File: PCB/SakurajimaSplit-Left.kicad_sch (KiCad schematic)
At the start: 53 parts, among them J1 SWD, J10 Conn_01x01_Pin, J11 Conn_01x01_Pin, J12 Conn_01x01_Pin, J13 Conn_01x01_Pin, J14 Conn_01x01_Pin, J15 Conn_01x01_Pin, J16 Conn_01x01_Pin, J17 Conn_01x01_Pin, J18 Conn_01x01_Pin, J2 USB-C to Right-Half, J3 Conn_01x01_Pin, J4 Conn_01x01_Pin, J5 Conn_01x01_Pin, J6 Conn_01x01_Pin, J7 Conn_01x01_Pin, J8 Conn_01x01_Pin, J9 Conn_01x01_Pin, SW1 SWCLK/BOOT0, SW2 Knob, U1 USBLC6-2SC6, U2 STM32G0B1CBT6, U3 ZJY_M233, Y1 8MHz

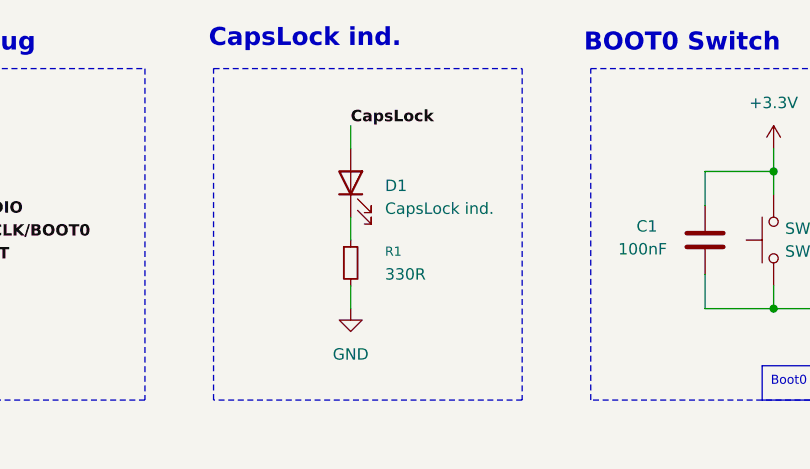
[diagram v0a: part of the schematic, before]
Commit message: fix(sch): fix matrix diode designators not starting from 1
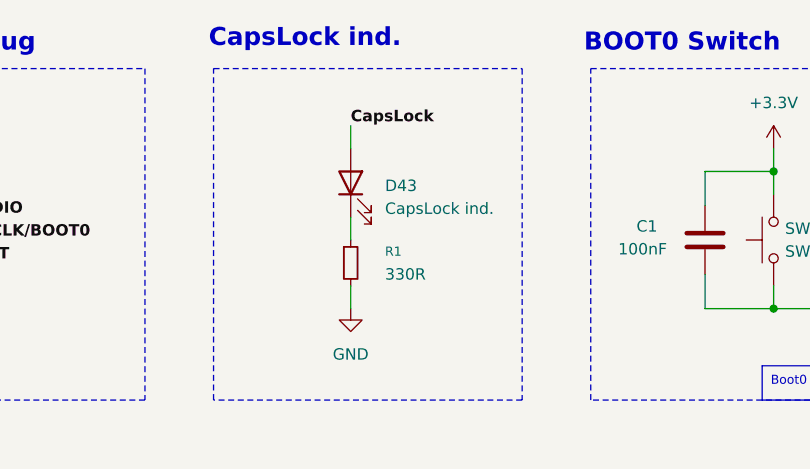
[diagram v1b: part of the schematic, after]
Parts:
- renumbered D1 to D43
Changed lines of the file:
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@@
 		(dnp no)
 		(fields_autoplaced yes)
-		(property "Reference" "D1"
+		(property "Reference" "D43"
 			(at 91.44 40.9574 90)
 			(effects
@@
 			(project ""
 				(path "/2049b6de-7453-46e1-ab60-70116abff9d6/d08add9a-e5d5-49be-809e-a90adb11436d"
-					(reference "D1")
+					(reference "D43")
 					(unit 1)
 				)

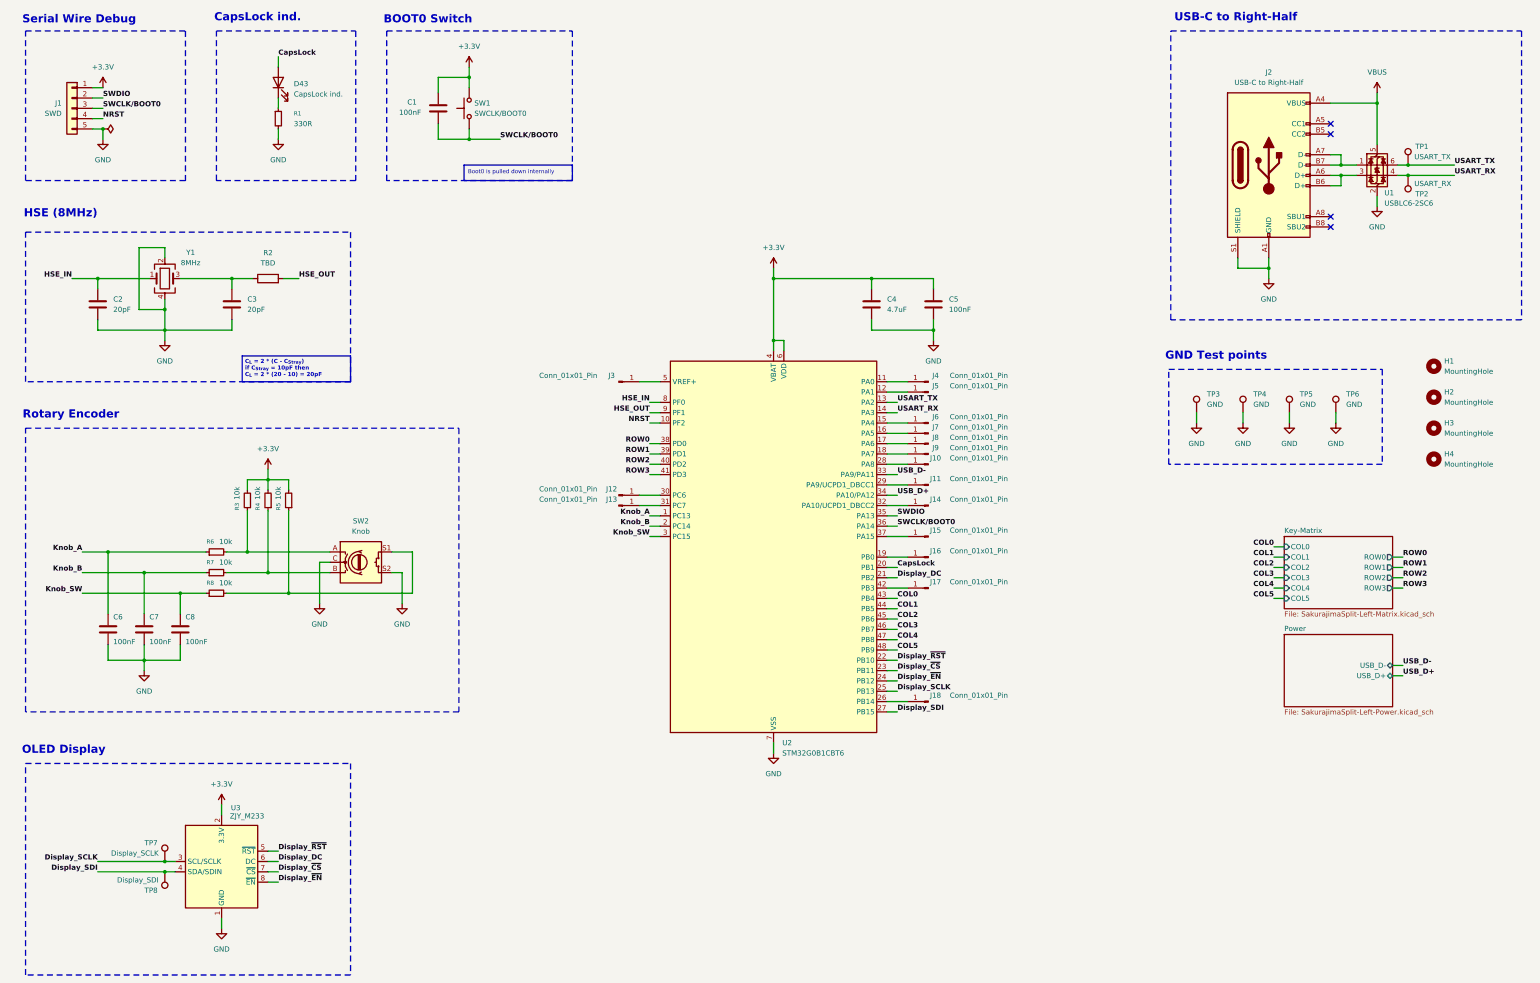
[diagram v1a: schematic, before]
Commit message: feat(sch): add spi flash, remove rotary encoder, fix footprints
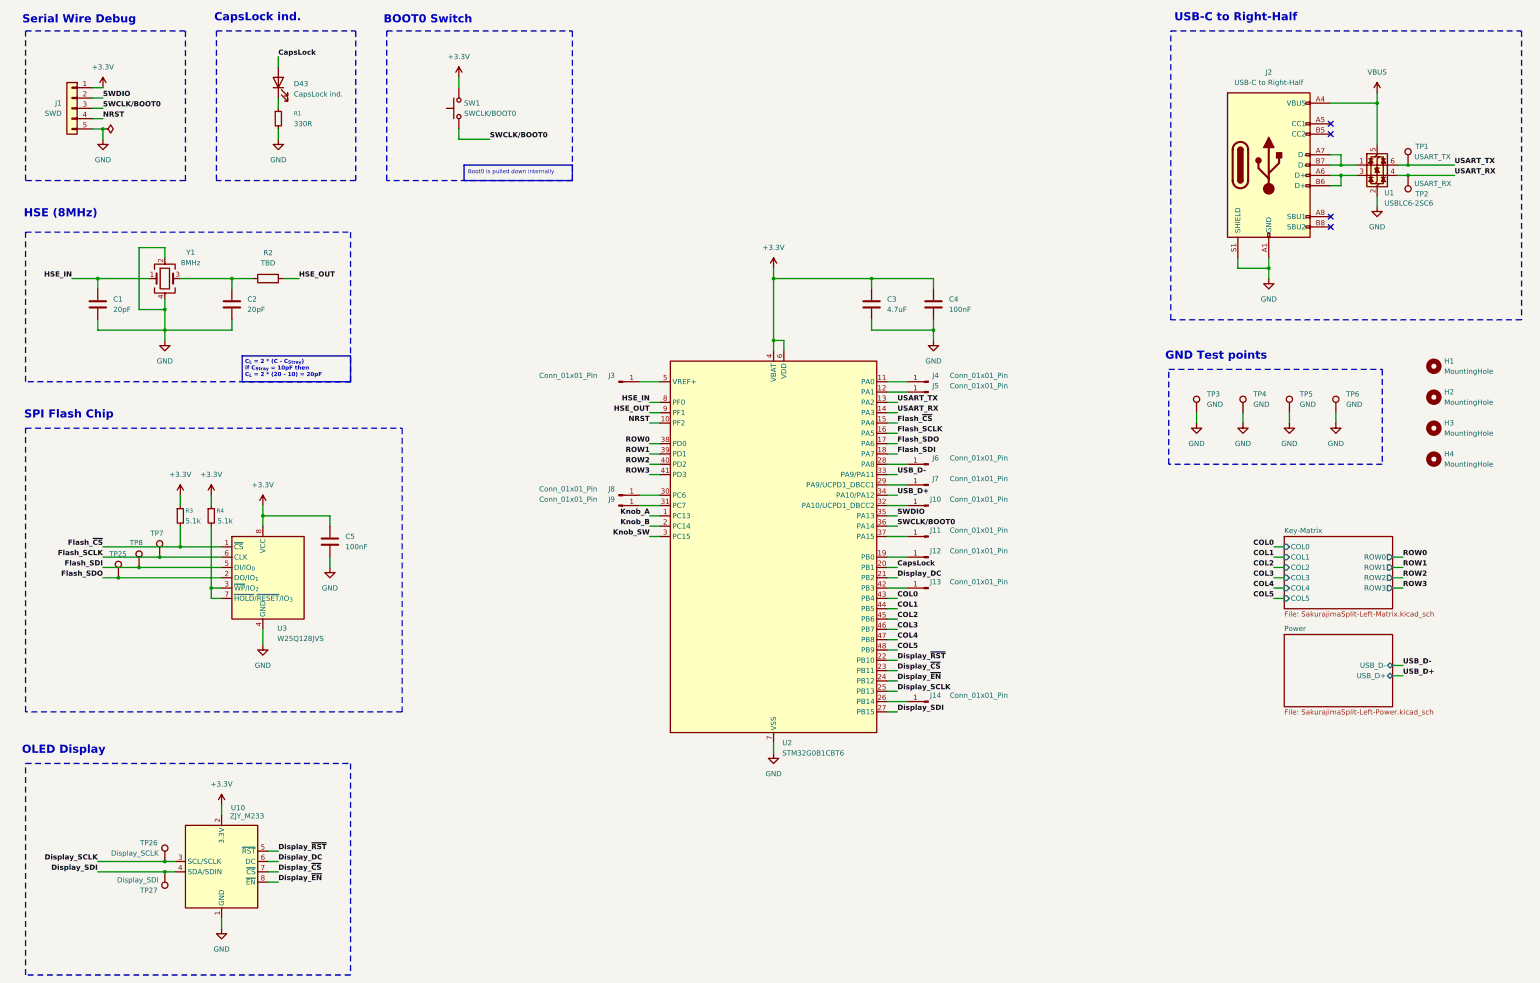
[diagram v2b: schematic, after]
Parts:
- removed C1, C6, C7, C8: 100nF, Capacitor_SMD:C_0603_1608Metric, symbol Device:C
- removed J6, J7, J8, J9: Conn_01x01_Pin, Connector_Wire:SolderWirePad_1x01_SMD_1x2mm, symbol Connector:Conn_01x01_Pin
- removed R5, R6, R7, R8: 10k, Resistor_SMD:R_0603_1608Metric, symbol Device:R_Small
- removed SW2: Knob, Rotary_Encoder:RotaryEncoder_Alps_EC11E-Switch_Vertical_H20mm, symbol Device:RotaryEncoder_Switch
- added C5: 100nF, Capacitor_SMD:C_0603_1608Metric, symbol Device:C
- added TP25: Flash_SDO, Hayata_Lib:TestPoint_Pad_Circular_1.3mm, symbol Connector:TestPoint
- added TP7: Flash_SCLK, Hayata_Lib:TestPoint_Pad_Circular_1.3mm, symbol Connector:TestPoint
- added TP8: Flash_SDI, Hayata_Lib:TestPoint_Pad_Circular_1.3mm, symbol Connector:TestPoint
- added U3: W25Q128JVS, Package_SO:SOIC-8_5.3x5.3mm_P1.27mm, symbol Memory_Flash:W25Q128JVS
- R3, R4: value 10k -> 5.1k; Distributor Link https://lionelectronic.ir/products/1219-CR0603FA1002G -> https://lionelectronic.ir/products/1212-0603WAF5101T5E; Manufacturer LIZ Electronics -> UniOhm; Manufacturer Part No. CR0603FA1002G -> 0603WAF5101T5E
- SW1: footprint Button_Switch_SMD:SW_Push_1P1T_XKB_TS-1187A -> Hayata_Lib:SW_Push_TS-1010B
- TP1, TP2, TP3, TP4, TP5, TP6: footprint TestPoint:TestPoint_Pad_2.0x2.0mm -> Hayata_Lib:TestPoint_Pad_Circular_1.3mm
- TP26: renamed from TP7; footprint TestPoint:TestPoint_Pad_2.0x2.0mm -> Hayata_Lib:TestPoint_Pad_Circular_1.3mm
- TP27: renamed from TP8; footprint TestPoint:TestPoint_Pad_2.0x2.0mm -> Hayata_Lib:TestPoint_Pad_Circular_1.3mm
- Y1: footprint Crystal:Crystal_SMD_3225-4Pin_3.2x2.5mm_HandSoldering -> Crystal:Crystal_SMD_3225-4Pin_3.2x2.5mm
- renumbered C2 to C1, C3 to C2, C4 to C3, C5 to C4, J14 to J10, J15 to J11, J16 to J12, J17 to J13, J18 to J14, J10 to J6, J11 to J7, J12 to J8, J13 to J9, U3 to U10
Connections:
- net +3.3V: now also R3.1, R4.1, C5.1, U3.8 (VCC); no longer R3.2, R4.2
- net GND: now also C5.2, U3.4 (GND)
- net Flash_~{CS}: now reaches U2.15 (PA4)
- net Flash_~{CS}: now also R3.2, U3.1 (~{CS})
- net Flash_SCLK: now reaches U2.16 (PA5)
- net Flash_SCLK: now also TP7.1, U3.6 (CLK)
- net Flash_SDO: now reaches U2.17 (PA6)
- net Flash_SDO: now also TP25.1, U3.2 (DO/IO_{1})
- net Flash_SDI: now reaches U2.18 (PA7)
- net Flash_SDI: now also TP8.1, U3.5 (DI/IO_{0})
- new net: R4.2, U3.3 (~{WP}/IO_{2}), U3.7 (~{HOLD}/~{RESET}/IO_{3})
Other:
- note added: "SPI Flash Chip"
- note removed: "Rotary Encoder"
- moved on the sheet: SW1

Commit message: fix(sch): remove encoder net labels, update mountinghole footprints
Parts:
- added J11, J12, J13: Conn_01x01_Pin, Connector_Wire:SolderWirePad_1x01_SMD_1x2mm, symbol Connector:Conn_01x01_Pin
- H1, H2, H3, H4: footprint MountingHole:MountingHole_3.2mm_M3_Pad -> MountingHole:MountingHole_3.2mm_M3_Pad_Via
- renumbered J11 to J14, J12 to J32, J13 to J33, J14 to J34
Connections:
- net Knob_A: no longer names the net of U2.1 (PC13)
- net Knob_A: now also J11.1 (Pin_1)
- net Knob_B: no longer names the net of U2.2 (PC14)
- net Knob_B: now also J12.1 (Pin_1)
- net Knob_SW: no longer names the net of U2.3 (PC15)
- net Knob_SW: now also J13.1 (Pin_1)
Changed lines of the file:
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@@
 	(wire
 		(pts
+			(xy 176.53 152.4) (xy 181.61 152.4)
+		)
+		(stroke
+			(width 0)
+			(type default)
+		)
+	)
+	(wire
+		(pts
 			(xy 71.12 165.1) (xy 71.12 167.64)
 		)
@@
 	(wire
 		(pts
-			(xy 179.07 149.86) (xy 181.61 149.86)
-		)
-		(stroke
-			(width 0)
-			(type default)
-		)
-	)
-	(wire
-		(pts
 			(xy 132.08 54.61) (xy 139.7 54.61)
 		)
@@
 	(wire
 		(pts
+			(xy 176.53 149.86) (xy 181.61 149.86)
+		)
+		(stroke
+			(width 0)
+			(type default)
+		)
+	)
+	(wire
+		(pts
 			(xy 87.63 44.45) (xy 87.63 46.99)
 		)
@@
 	(wire
 		(pts
+			(xy 176.53 147.32) (xy 181.61 147.32)
+		)
+		(stroke
+			(width 0)
+			(type default)
+		)
+	)
+	(wire
+		(pts
 			(xy 179.07 129.54) (xy 181.61 129.54)
 		)
@@
 	(wire
 		(pts
-			(xy 179.07 152.4) (xy 181.61 152.4)
-		)
-		(stroke
-			(width 0)
-			(type default)
-		)
-	)
-	(wire
-		(pts
 			(xy 358.14 45.72) (xy 358.14 55.88)
 		)
@@
 	(wire
 		(pts
-			(xy 179.07 147.32) (xy 181.61 147.32)
-		)
-		(stroke
-			(width 0)
-			(type default)
-		)
-	)
-	(wire
-		(pts
 			(xy 364.49 162.56) (xy 361.95 162.56)
 		)
@@
 		)
 	)
-	(label "Knob_SW"
-		(at 179.07 152.4 180)
-		(effects
-			(font
-				(size 1.27 1.27)
-				(thickness 0.254)
-				(bold yes)
-			)
-			(justify right bottom)
-		)
-	)
 	(label "COL0"
 		(at 332.74 154.94 180)
@@
 		)
 	)
-	(label "Knob_B"
-		(at 179.07 149.86 180)
-		(effects
-			(font
-				(size 1.27 1.27)
-				(thickness 0.254)
-				(bold yes)
-			)
-			(justify right bottom)
-		)
-	)
 	(label "ROW1"
 		(at 179.07 132.08 180)
@@
 		)
 	)
-	(label "Knob_A"
-		(at 179.07 147.32 180)
-		(effects
-			(font
-				(size 1.27 1.27)
-				(thickness 0.254)
-				(bold yes)
-			)
-			(justify right bottom)
-		)
-	)
 	(label "COL5"
 		(at 332.74 167.64 180)
@@
 			)
 		)
-		(property "Footprint" "MountingHole:MountingHole_3.2mm_M3_Pad"
+		(property "Footprint" "MountingHole:MountingHole_3.2mm_M3_Pad_Via"
 			(at 372.11 118.11 0)
 			(effects
@@
 		(on_board yes)
 		(dnp no)
-		(property "Reference" "J13"
+		(property "Reference" "J33"
 			(at 249.428 163.576 0)
 			(effects
@@
 			(project "SakurajimaSplit"
 				(path "/2049b6de-7453-46e1-ab60-70116abff9d6/d08add9a-e5d5-49be-809e-a90adb11436d"
-					(reference "J13")
+					(reference "J33")
 					(unit 1)
 				)
@@
 		(on_board yes)
 		(dnp no)
-		(property "Reference" "J12"
+		(property "Reference" "J32"
 			(at 249.428 155.956 0)
 			(effects
@@
 			(project "SakurajimaSplit"
 				(path "/2049b6de-7453-46e1-ab60-70116abff9d6/d08add9a-e5d5-49be-809e-a90adb11436d"
-					(reference "J12")
+					(reference "J32")
 					(unit 1)
 				)
@@
 		(on_board yes)
 		(dnp no)
-		(property "Reference" "J14"
+		(property "Reference" "J34"
 			(at 249.428 191.516 0)
 			(effects
@@
 			(project "SakurajimaSplit"
 				(path "/2049b6de-7453-46e1-ab60-70116abff9d6/d08add9a-e5d5-49be-809e-a90adb11436d"
-					(reference "J14")
+					(reference "J34")
 					(unit 1)
 				)
@@
 			)
 		)
-		(property "Footprint" "MountingHole:MountingHole_3.2mm_M3_Pad"
+		(property "Footprint" "MountingHole:MountingHole_3.2mm_M3_Pad_Via"
 			(at 372.11 110.49 0)
 			(effects
@@
 	)
 	(symbol
+		(lib_id "Connector:Conn_01x01_Pin")
+		(at 171.45 149.86 0)
+		(mirror x)
+		(unit 1)
+		(exclude_from_sim no)
+		(in_bom no)
+		(on_board yes)
+		(dnp no)
+		(property "Reference" "J12"
+			(at 169.672 148.336 0)
+			(effects
+				(font
+					(size 1.27 1.27)
+				)
+			)
+		)
+		(property "Value" "Conn_01x01_Pin"
+			(at 159.004 148.336 0)
+			(effects
+				(font
+					(size 1.27 1.27)
+				)
+			)
+		)
+		(property "Footprint" "Connector_Wire:SolderWirePad_1x01_SMD_1x2mm"
+			(at 171.45 149.86 0)
+			(effects
+				(font
+					(size 1.27 1.27)
+					(thickness 0.254)
+					(bold yes)
+				)
+				(hide yes)
+			)
+		)
+		(property "Datasheet" "~"
+			(at 171.45 149.86 0)
+			(effects
+				(font
+					(size 1.27 1.27)
+					(thickness 0.254)
+					(bold yes)
+				)
+				(hide yes)
+			)
+		)
+		(property "Description" "Generic connector, single row, 01x01, script generated"
+			(at 171.45 149.86 0)
+			(effects
+				(font
+					(size 1.27 1.27)
+					(thickness 0.254)
+					(bold yes)
+				)
+				(hide yes)
+			)
+		)
+		(pin "1"
+		)
+		(instances
+			(project "SakurajimaSplit"
+				(path "/2049b6de-7453-46e1-ab60-70116abff9d6/d08add9a-e5d5-49be-809e-a90adb11436d"
+					(reference "J12")
+					(unit 1)
+				)
+			)
+		)
+	)
+	(symbol
 		(lib_id "Device:R")
 		(at 85.09 88.9 90)
@@
 	(symbol
 		(lib_id "Connector:Conn_01x01_Pin")
+		(at 171.45 152.4 0)
+		(mirror x)
+		(unit 1)
+		(exclude_from_sim no)
+		(in_bom no)
+		(on_board yes)
+		(dnp no)
+		(property "Reference" "J13"
+			(at 169.672 150.876 0)
+			(effects
+				(font
+					(size 1.27 1.27)
+				)
+			)
+		)
+		(property "Value" "Conn_01x01_Pin"
+			(at 159.004 150.876 0)
+			(effects
+				(font
+					(size 1.27 1.27)
+				)
+			)
+		)
+		(property "Footprint" "Connector_Wire:SolderWirePad_1x01_SMD_1x2mm"
+			(at 171.45 152.4 0)
+			(effects
+				(font
+					(size 1.27 1.27)
+					(thickness 0.254)
+					(bold yes)
+				)
+				(hide yes)
+			)
+		)
+		(property "Datasheet" "~"
+			(at 171.45 152.4 0)
+			(effects
+				(font
+					(size 1.27 1.27)
+					(thickness 0.254)
+					(bold yes)
+				)
+				(hide yes)
+			)
+		)
+		(property "Description" "Generic connector, single row, 01x01, script generated"
+			(at 171.45 152.4 0)
+			(effects
+				(font
+					(size 1.27 1.27)
+					(thickness 0.254)
+					(bold yes)
+				)
+				(hide yes)
+			)
+		)
+		(pin "1"
+		)
+		(instances
+			(project "SakurajimaSplit"
+				(path "/2049b6de-7453-46e1-ab60-70116abff9d6/d08add9a-e5d5-49be-809e-a90adb11436d"
+					(reference "J13")
+					(unit 1)
+				)
+			)
+		)
+	)
+	(symbol
+		(lib_id "Connector:Conn_01x01_Pin")
 		(at 247.65 114.3 180)
 		(unit 1)
@@
 	)
 	(symbol
+		(lib_id "Connector:Conn_01x01_Pin")
+		(at 171.45 147.32 0)
+		(mirror x)
+		(unit 1)
+		(exclude_from_sim no)
+		(in_bom no)
+		(on_board yes)
+		(dnp no)
+		(property "Reference" "J11"
+			(at 169.672 145.796 0)
+			(effects
+				(font
+					(size 1.27 1.27)
+				)
+			)
+		)
+		(property "Value" "Conn_01x01_Pin"
+			(at 159.004 145.796 0)
+			(effects
+				(font
+					(size 1.27 1.27)
+				)
+			)
+		)
+		(property "Footprint" "Connector_Wire:SolderWirePad_1x01_SMD_1x2mm"
+			(at 171.45 147.32 0)
+			(effects
+				(font
+					(size 1.27 1.27)
+					(thickness 0.254)
+					(bold yes)
+				)
+				(hide yes)
+			)
+		)
+		(property "Datasheet" "~"
+			(at 171.45 147.32 0)
+			(effects
+				(font
+					(size 1.27 1.27)
+					(thickness 0.254)
+					(bold yes)
+				)
+				(hide yes)
+			)
+		)
+		(property "Description" "Generic connector, single row, 01x01, script generated"
+			(at 171.45 147.32 0)
+			(effects
+				(font
+					(size 1.27 1.27)
+					(thickness 0.254)
+					(bold yes)
+				)
+				(hide yes)
+			)
+		)
+		(pin "1"
+		)
+		(instances
+			(project "SakurajimaSplit"
+				(path "/2049b6de-7453-46e1-ab60-70116abff9d6/d08add9a-e5d5-49be-809e-a90adb11436d"
+					(reference "J11")
+					(unit 1)
+				)
+			)
+		)
+	)
+	(symbol
 		(lib_id "Device:C")
 		(at 100.33 153.67 0)
@@
 			)
 		)
-		(property "Footprint" "MountingHole:MountingHole_3.2mm_M3_Pad"
+		(property "Footprint" "MountingHole:MountingHole_3.2mm_M3_Pad_Via"
 			(at 372.11 125.73 0)
 			(effects
@@
 		(on_board yes)
 		(dnp no)
-		(property "Reference" "J11"
+		(property "Reference" "J14"
 			(at 249.428 150.876 0)
 			(effects
@@
 			(project "SakurajimaSplit"
 				(path "/2049b6de-7453-46e1-ab60-70116abff9d6/d08add9a-e5d5-49be-809e-a90adb11436d"
-					(reference "J11")
+					(reference "J14")
 					(unit 1)
 				)
@@
 			)
 		)
-		(property "Footprint" "MountingHole:MountingHole_3.2mm_M3_Pad"
+		(property "Footprint" "MountingHole:MountingHole_3.2mm_M3_Pad_Via"
 			(at 372.11 133.35 0)
 			(effects
